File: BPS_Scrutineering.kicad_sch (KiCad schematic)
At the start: 50 parts, among them J1 Conn_01x01_Female, J10 Conn_01x01_Female, J11 Conn_01x01_Female, J12 Conn_01x01_Female, J13 Conn_01x01_Female, J14 Conn_01x01_Female, J2 Conn_01x01_Female, J3 Conn_01x01_Female, J4 Conn_01x01_Female, J5 Conn_01x01_Female, J6 Conn_01x01_Female, J7 Conn_01x01_Female, J8 Conn_01x01_Female, J9 Conn_01x01_Female, SW1 SW_DIP_x07, SW2 SW_DIP_x07

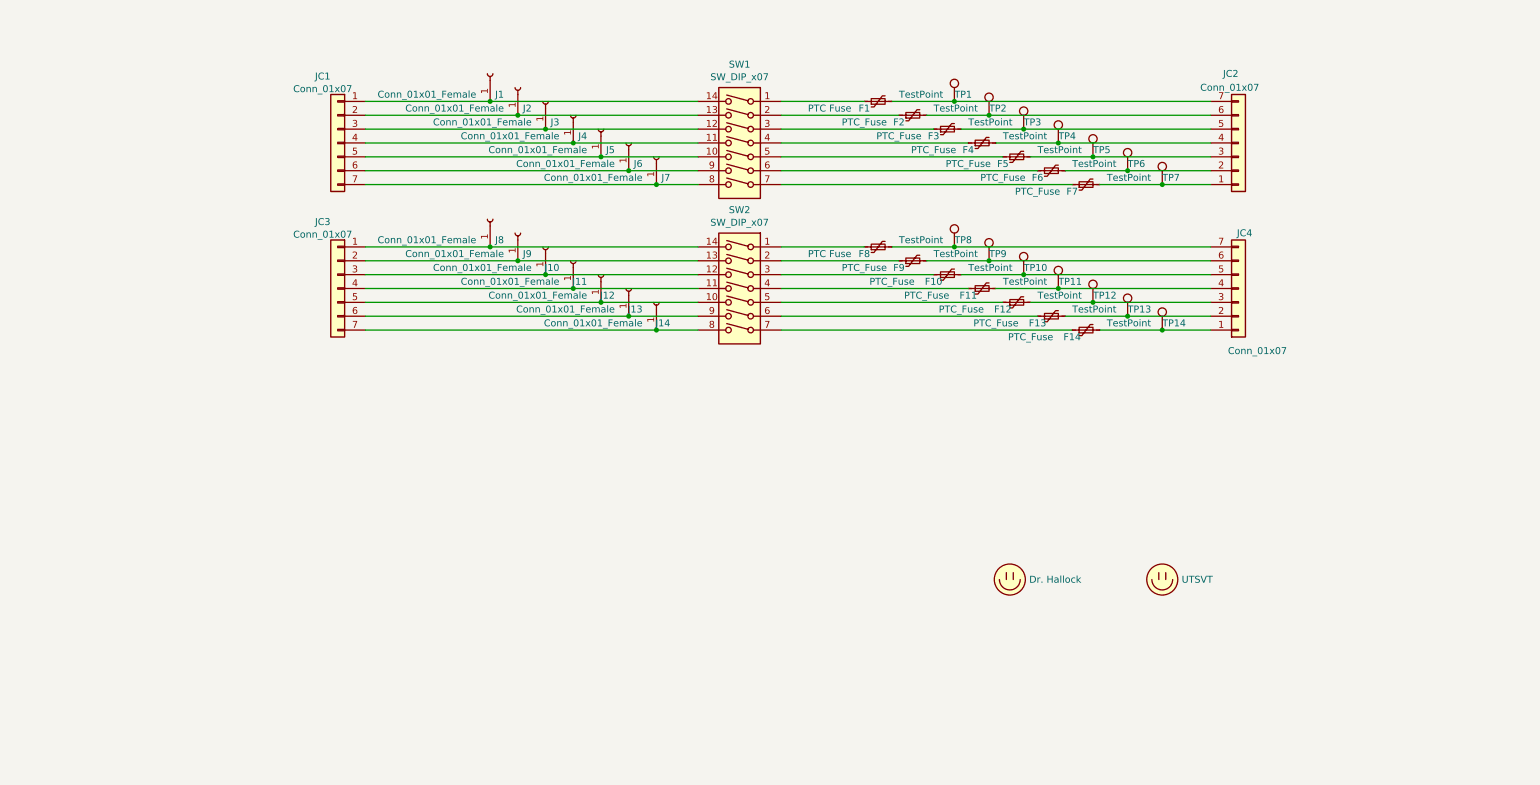
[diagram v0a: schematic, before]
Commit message: Added PTC fuses along all molex connectors, updated datasheet links, and updated component footprints
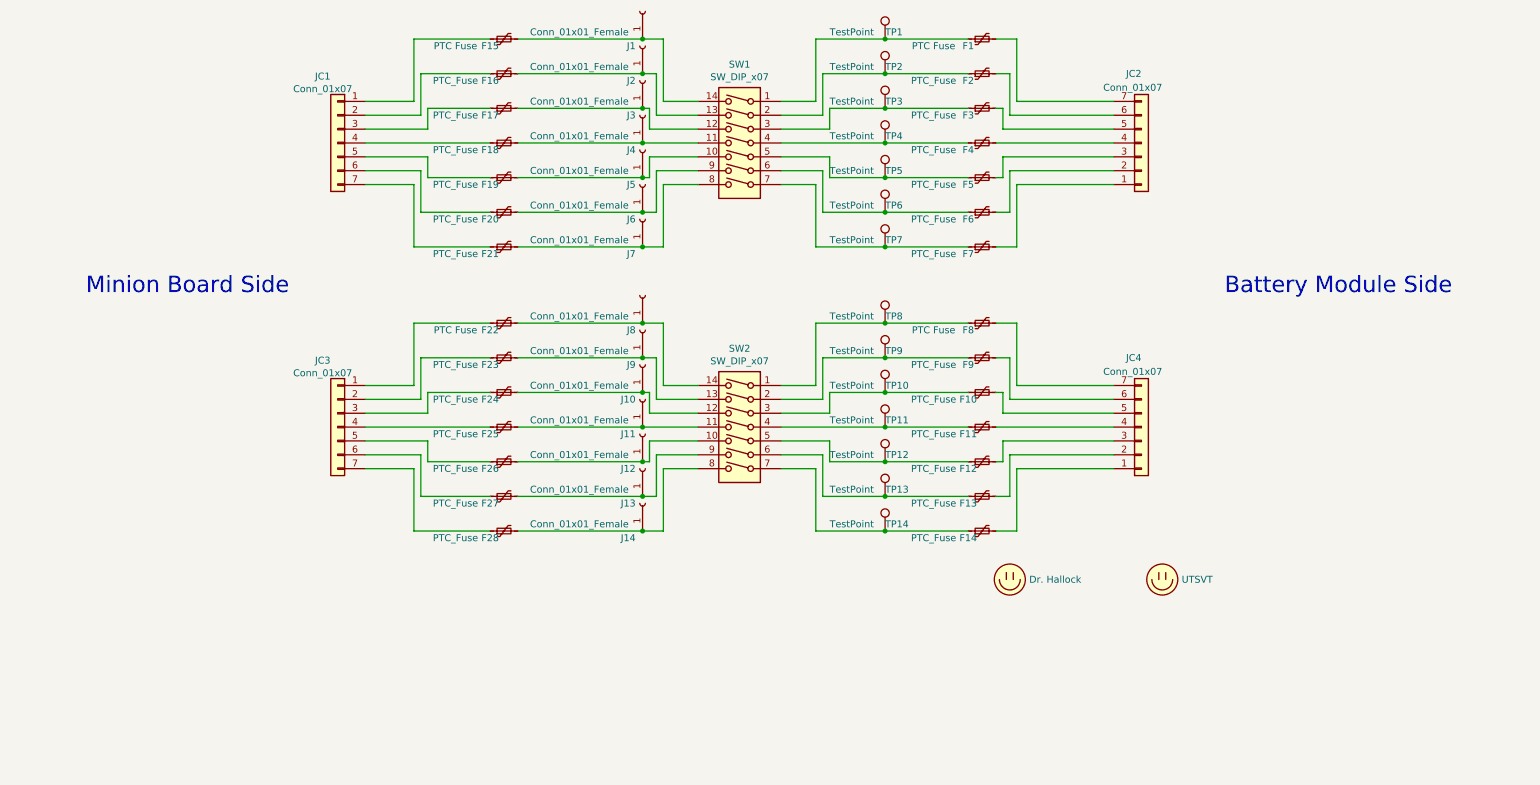
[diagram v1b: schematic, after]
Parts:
- added F15, F22: PTC Fuse, UTSVT_Special:ptc_fuse_FUSC1607X75N, symbol Device:Polyfuse_Small
- added F16, F17, F18, F19, F20, F21, F23, F24, F25, F26, F27, F28: PTC_Fuse, UTSVT_Special:ptc_fuse_FUSC1607X75N, symbol Device:Polyfuse_Small
- F1, F10, F11, F12, F13, F14, F2, F3, F4, F5, F6, F7, F8, F9: footprint (none) -> UTSVT_Special:ptc_fuse_FUSC1607X75N
- J1, J10, J11, J12, J13, J14, J2, J3, J4, J5, J6, J7, J8, J9: footprint UTSVT_Connectors:Banana_Jack_1_Pin_4mm -> UTSVT_Connectors:Cal_Test_Banana_Jack_1_Pin_4mm
- JC1, JC2, JC3, JC4: footprint UTSVT_Connectors:Molex_MicroFit_01x07_Horizontal -> UTSVT_Connectors:Molex_Microfit+_01x07_Horizontal
- SW1, SW2: footprint Button_Switch_SMD:SW_DIP_SPSTx07_Slide_6.7x19.34mm_W6.73mm_P2.54mm_LowProfile_JPin -> UTSVT_Special:7switch_module_DS04254207BKSMT
- TP1, TP10, TP11, TP12, TP13, TP14, TP2, TP3, TP4, TP5, TP6, TP7, TP8, TP9: footprint (none) -> TestPoint:TestPoint_THTPad_D2.0mm_Drill1.0mm
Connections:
- net at J1.1 (Pin_1), SW1.14: now also F15.2; no longer JC1.1 (Pin_1)
- net at J2.1 (Pin_1), SW1.13: now also F16.2; no longer JC1.2 (Pin_2)
- net at J3.1 (Pin_1), SW1.12: now also F17.2; no longer JC1.3 (Pin_3)
- net at J4.1 (Pin_1), SW1.11: now also F18.2; no longer JC1.4 (Pin_4)
- net at J5.1 (Pin_1), SW1.10: now also F19.2; no longer JC1.5 (Pin_5)
- net at J6.1 (Pin_1), SW1.9: now also F20.2; no longer JC1.6 (Pin_6)
- net at J7.1 (Pin_1), SW1.8: now also F21.2; no longer JC1.7 (Pin_7)
- net at J8.1 (Pin_1), SW2.14: now also F22.2; no longer JC3.1 (Pin_1)
- net at J9.1 (Pin_1), SW2.13: now also F23.2; no longer JC3.2 (Pin_2)
- net at J10.1 (Pin_1), SW2.12: now also F24.2; no longer JC3.3 (Pin_3)
- net at J11.1 (Pin_1), SW2.11: now also F25.2; no longer JC3.4 (Pin_4)
- net at J12.1 (Pin_1), SW2.10: now also F26.2; no longer JC3.5 (Pin_5)
- net at J13.1 (Pin_1), SW2.9: now also F27.2; no longer JC3.6 (Pin_6)
- net at J14.1 (Pin_1), SW2.8: now also F28.2; no longer JC3.7 (Pin_7)
- net at F7.2, JC2.1 (Pin_1): no longer TP7.1
- net at F6.2, JC2.2 (Pin_2): no longer TP6.1
- net at F5.2, JC2.3 (Pin_3): no longer TP5.1
- net at F4.2, JC2.4 (Pin_4): no longer TP4.1
- net at F3.2, JC2.5 (Pin_5): no longer TP3.1
- net at F2.2, JC2.6 (Pin_6): no longer TP2.1
- net at F1.2, JC2.7 (Pin_7): no longer TP1.1
- net at F14.2, JC4.1 (Pin_1): no longer TP14.1
- net at F13.2, JC4.2 (Pin_2): no longer TP13.1
- net at F12.2, JC4.3 (Pin_3): no longer TP12.1
- net at F11.2, JC4.4 (Pin_4): no longer TP11.1
- net at F10.2, JC4.5 (Pin_5): no longer TP10.1
- net at F9.2, JC4.6 (Pin_6): no longer TP9.1
- net at F8.2, JC4.7 (Pin_7): no longer TP8.1
- net at F1.1, SW1.1: now also TP1.1
- net at F2.1, SW1.2: now also TP2.1
- net at F3.1, SW1.3: now also TP3.1
- net at F4.1, SW1.4: now also TP4.1
- net at F5.1, SW1.5: now also TP5.1
- net at F6.1, SW1.6: now also TP6.1
- net at F7.1, SW1.7: now also TP7.1
- net at F8.1, SW2.1: now also TP8.1
- net at F9.1, SW2.2: now also TP9.1
- net at F10.1, SW2.3: now also TP10.1
- net at F11.1, SW2.4: now also TP11.1
- net at F12.1, SW2.5: now also TP12.1
- net at F13.1, SW2.6: now also TP13.1
- net at F14.1, SW2.7: now also TP14.1
- new net: F15.1, JC1.1 (Pin_1)
- new net: F16.1, JC1.2 (Pin_2)
- new net: F17.1, JC1.3 (Pin_3)
- new net: F18.1, JC1.4 (Pin_4)
- new net: F19.1, JC1.5 (Pin_5)
- new net: F20.1, JC1.6 (Pin_6)
- new net: F21.1, JC1.7 (Pin_7)
- new net: F26.1, JC3.5 (Pin_5)
- new net: F27.1, JC3.6 (Pin_6)
- new net: F24.1, JC3.3 (Pin_3)
- new net: F28.1, JC3.7 (Pin_7)
- new net: F23.1, JC3.2 (Pin_2)
- new net: F22.1, JC3.1 (Pin_1)
- new net: F25.1, JC3.4 (Pin_4)
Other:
- note added: "Battery Module Side"
- note added: "Minion Board Side"
- moved on the sheet: F1, F2, F3, F5, F6, F7, J1, J2, J3, J4, J5, J6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

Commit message: Almost done with laying out the PCB. Replaced the banana connectors with test points
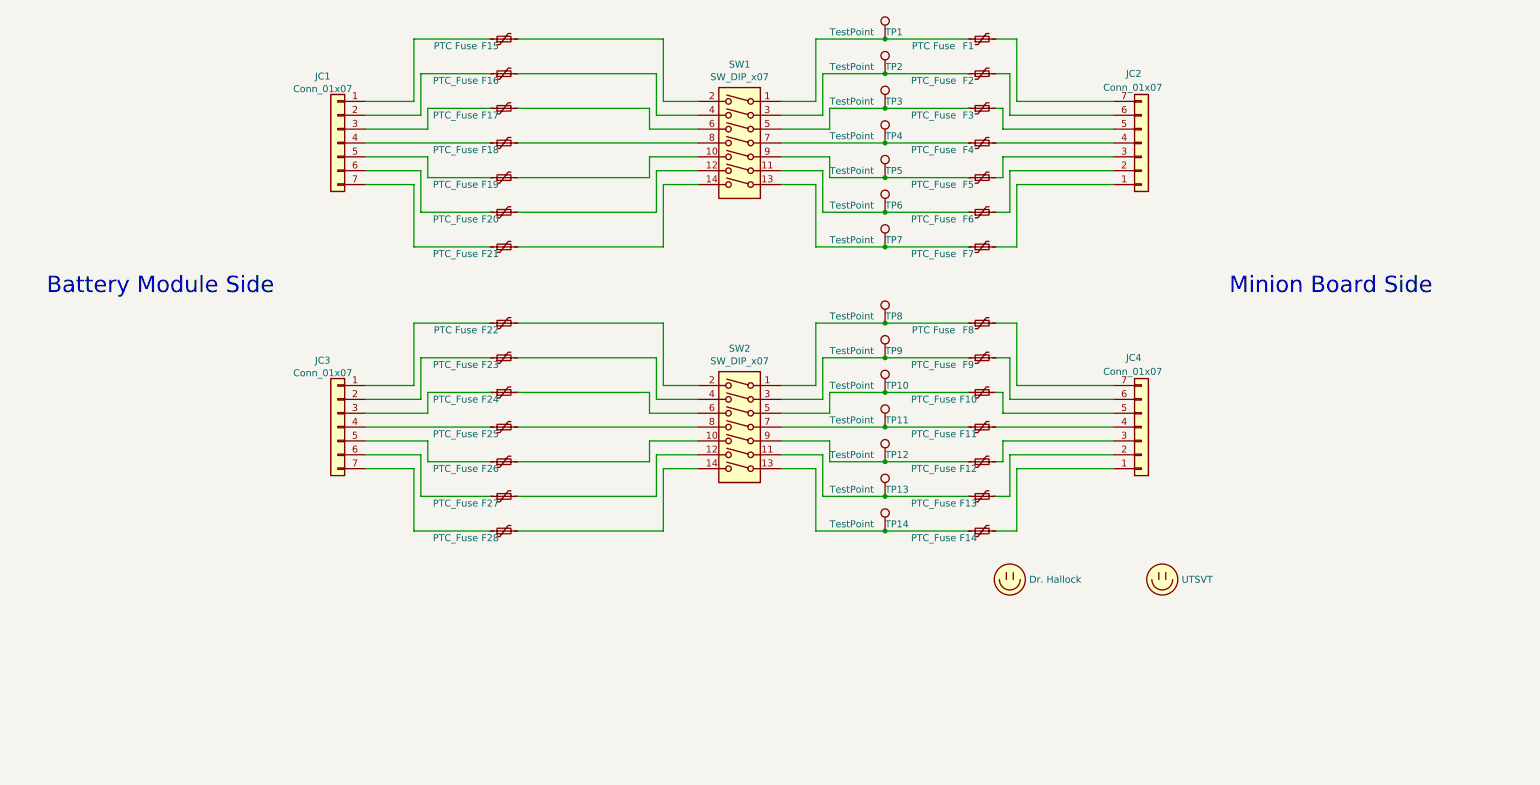
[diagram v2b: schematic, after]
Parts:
- removed J1, J10, J11, J12, J13, J14, J2, J3, J4, J5, J6, J7, J8, J9: Conn_01x01_Female, UTSVT_Connectors:Cal_Test_Banana_Jack_1_Pin_4mm, symbol Connector:Conn_01x01_Female
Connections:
- net at SW1.14: now also F21.2; no longer F15.2
- net at SW1.13: now also F7.1, TP7.1; no longer F16.2
- net at SW1.11: now also F6.1, TP6.1; no longer F18.2
- net at SW1.12: now also F20.2; no longer F17.2
- net at F2.1, TP2.1: now also SW1.3; no longer SW1.2
- net at F3.1, TP3.1: now also SW1.5; no longer SW1.3
- net at F4.1, TP4.1: now also SW1.7; no longer SW1.4
- net at F5.1, TP5.1: now also SW1.9; no longer SW1.5
- net at SW1.8: now also F18.2; no longer F21.2
- net at SW2.11: now also F13.1, TP13.1; no longer F25.2
- net at SW2.12: now also F27.2; no longer F24.2
- net at SW2.13: now also F14.1, TP14.1; no longer F23.2
- net at SW2.14: now also F28.2; no longer F22.2
- net at F9.1, TP9.1: now also SW2.3; no longer SW2.2
- net at F10.1, TP10.1: now also SW2.5; no longer SW2.3
- net at F11.1, TP11.1: now also SW2.7; no longer SW2.4
- net at F12.1, TP12.1: now also SW2.9; no longer SW2.5
- net at SW2.8: now also F25.2; no longer F28.2
- new net: F15.2, SW1.2
- new net: F16.2, SW1.4
- new net: F17.2, SW1.6
- new net: F22.2, SW2.2
- new net: F23.2, SW2.4
- new net: F24.2, SW2.6

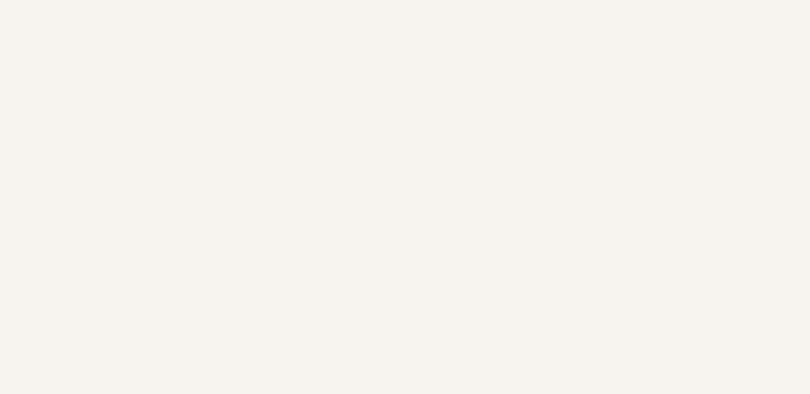
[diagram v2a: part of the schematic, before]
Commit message: Complete draft of PCB layout
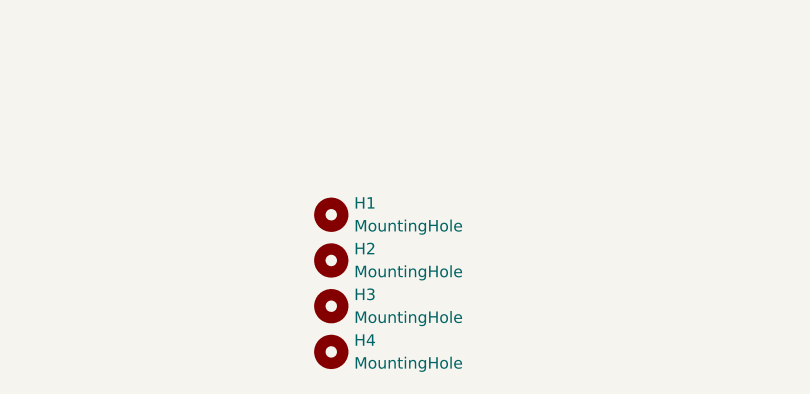
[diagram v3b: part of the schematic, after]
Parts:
- added H1, H2, H3, H4: MountingHole, MountingHole:MountingHole_3mm_Pad, symbol Mechanical:MountingHole
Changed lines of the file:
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@@
     (pin "7")
+  )
+  (symbol (lib_id "Mechanical:MountingHole") (at 119.38 186.69 0) (unit 1)
+    (in_bom yes) (on_board yes) (fields_autoplaced)
+    (property "Reference" "H4" (id 0) (at 121.92 185.4199 0)
+      (effects (font (size 1.27 1.27)) (justify left))
+    )
+    (property "Value" "MountingHole" (id 1) (at 121.92 187.9599 0)
+      (effects (font (size 1.27 1.27)) (justify left))
+    )
+    (property "Footprint" "MountingHole:MountingHole_3mm_Pad" (id 2) (at 119.38 186.69 0)
+      (effects (font (size 1.27 1.27)) hide)
+    )
+    (property "Datasheet" "~" (id 3) (at 119.38 186.69 0)
+      (effects (font (size 1.27 1.27)) hide)
+    )
   )
   (symbol (lib_id "Connector:TestPoint") (at 170.18 80.01 0) (unit 1)
@@
     (pin "2")
   )
+  (symbol (lib_id "Mechanical:MountingHole") (at 119.38 176.53 0) (unit 1)
+    (in_bom yes) (on_board yes) (fields_autoplaced)
+    (property "Reference" "H2" (id 0) (at 121.92 175.2599 0)
+      (effects (font (size 1.27 1.27)) (justify left))
+    )
+    (property "Value" "MountingHole" (id 1) (at 121.92 177.7999 0)
+      (effects (font (size 1.27 1.27)) (justify left))
+    )
+    (property "Footprint" "MountingHole:MountingHole_3mm_Pad" (id 2) (at 119.38 176.53 0)
+      (effects (font (size 1.27 1.27)) hide)
+    )
+    (property "Datasheet" "~" (id 3) (at 119.38 176.53 0)
+      (effects (font (size 1.27 1.27)) hide)
+    )
+  )
   (symbol (lib_id "Device:Polyfuse_Small") (at 100.33 119.38 90) (unit 1)
     (in_bom yes) (on_board yes)
@@
     (pin "2")
   )
+  (symbol (lib_id "Mechanical:MountingHole") (at 119.38 171.45 0) (unit 1)
+    (in_bom yes) (on_board yes) (fields_autoplaced)
+    (property "Reference" "H1" (id 0) (at 121.92 170.1799 0)
+      (effects (font (size 1.27 1.27)) (justify left))
+    )
+    (property "Value" "MountingHole" (id 1) (at 121.92 172.7199 0)
+      (effects (font (size 1.27 1.27)) (justify left))
+    )
+    (property "Footprint" "MountingHole:MountingHole_3mm_Pad" (id 2) (at 119.38 171.45 0)
+      (effects (font (size 1.27 1.27)) hide)
+    )
+    (property "Datasheet" "~" (id 3) (at 119.38 171.45 0)
+      (effects (font (size 1.27 1.27)) hide)
+    )
+  )
   (symbol (lib_id "Connector:TestPoint") (at 170.18 106.68 0) (unit 1)
     (in_bom yes) (on_board yes)
@@
     (pin "1")
     (pin "2")
+  )
+  (symbol (lib_id "Mechanical:MountingHole") (at 119.38 181.61 0) (unit 1)
+    (in_bom yes) (on_board yes) (fields_autoplaced)
+    (property "Reference" "H3" (id 0) (at 121.92 180.3399 0)
+      (effects (font (size 1.27 1.27)) (justify left))
+    )
+    (property "Value" "MountingHole" (id 1) (at 121.92 182.8799 0)
+      (effects (font (size 1.27 1.27)) (justify left))
+    )
+    (property "Footprint" "MountingHole:MountingHole_3mm_Pad" (id 2) (at 119.38 181.61 0)
+      (effects (font (size 1.27 1.27)) hide)
+    )
+    (property "Datasheet" "~" (id 3) (at 119.38 181.61 0)
+      (effects (font (size 1.27 1.27)) hide)
+    )
   )
   (symbol (lib_id "Device:Polyfuse_Small") (at 100.33 106.68 90) (unit 1)
@@
       (reference "F28") (unit 1) (value "PTC_Fuse") (footprint "UTSVT_Special:ptc_fuse_FUSC1607X75N")
     )
+    (path "/75864b11-2524-482a-8b45-7c4675cc5e1f"
+      (reference "H1") (unit 1) (value "MountingHole") (footprint "MountingHole:MountingHole_3mm_Pad")
+    )
+    (path "/64fbf4fe-e1aa-4755-950e-03043a1a2c9c"
+      (reference "H2") (unit 1) (value "MountingHole") (footprint "MountingHole:MountingHole_3mm_Pad")
+    )
+    (path "/db2858f4-d7f7-417f-a045-bd87dcc8080c"
+      (reference "H3") (unit 1) (value "MountingHole") (footprint "MountingHole:MountingHole_3mm_Pad")
+    )
+    (path "/0e147d9c-439d-4d5f-9428-a11629deed92"
+      (reference "H4") (unit 1) (value "MountingHole") (footprint "MountingHole:MountingHole_3mm_Pad")
+    )
     (path "/00000000-0000-0000-0000-00005f94ef32"
